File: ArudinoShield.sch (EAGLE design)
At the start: 25 parts, among them IC1 L298

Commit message: added ground plane, updated layout
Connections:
- removed net N$13: B1.GND@0, HC05.3, R2.1
- net GND: now also B1.GND@0, HC05.3, R2.1
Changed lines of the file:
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@@
-</segment>
-</net>
-<net name="N$13" class="0">
-<segment>
-<wire x1="109.22" y1="73.66" x2="109.22" y2="17.78" width="0.1524" layer="91"/>
-<wire x1="109.22" y1="17.78" x2="83.82" y2="17.78" width="0.1524" layer="91"/>
-<pinref part="B1" gate="G$1" pin="GND@0"/>
-<wire x1="83.82" y1="17.78" x2="50.8" y2="17.78" width="0.1524" layer="91"/>
-<wire x1="50.8" y1="17.78" x2="50.8" y2="30.48" width="0.1524" layer="91"/>
-<pinref part="R2" gate="G$1" pin="1"/>
-<wire x1="83.82" y1="27.94" x2="83.82" y2="17.78" width="0.1524" layer="91"/>
-<junction x="83.82" y="17.78"/>
-<pinref part="HC05" gate="A" pin="3"/>
-<wire x1="114.3" y1="73.66" x2="109.22" y2="73.66" width="0.1524" layer="91"/>
 </segment>
 </net>
@@
 <junction x="45.72" y="30.48"/>
 </segment>
-</net>
+<segment>
+<wire x1="109.22" y1="73.66" x2="109.22" y2="17.78" width="0.1524" layer="91"/>
+<wire x1="109.22" y1="17.78" x2="83.82" y2="17.78" width="0.1524" layer="91"/>
+<pinref part="B1" gate="G$1" pin="GND@0"/>
+<wire x1="83.82" y1="17.78" x2="50.8" y2="17.78" width="0.1524" layer="91"/>
+<wire x1="50.8" y1="17.78" x2="50.8" y2="30.48" width="0.1524" layer="91"/>
+<pinref part="R2" gate="G$1" pin="1"/>
+<wire x1="83.82" y1="27.94" x2="83.82" y2="17.78" width="0.1524" layer="91"/>
+<junction x="83.82" y="17.78"/>
+<pinref part="HC05" gate="A" pin="3"/>
+<wire x1="114.3" y1="73.66" x2="109.22" y2="73.66" width="0.1524" layer="91"/>
+</segment>
+</net>

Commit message: updated board and previews
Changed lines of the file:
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@@
 <pinref part="HC05" gate="A" pin="3"/>
 <wire x1="114.3" y1="73.66" x2="109.22" y2="73.66" width="0.1524" layer="91"/>
+<label x="50.8" y="17.78" size="1.6764" layer="95"/>
 </segment>
 </net>

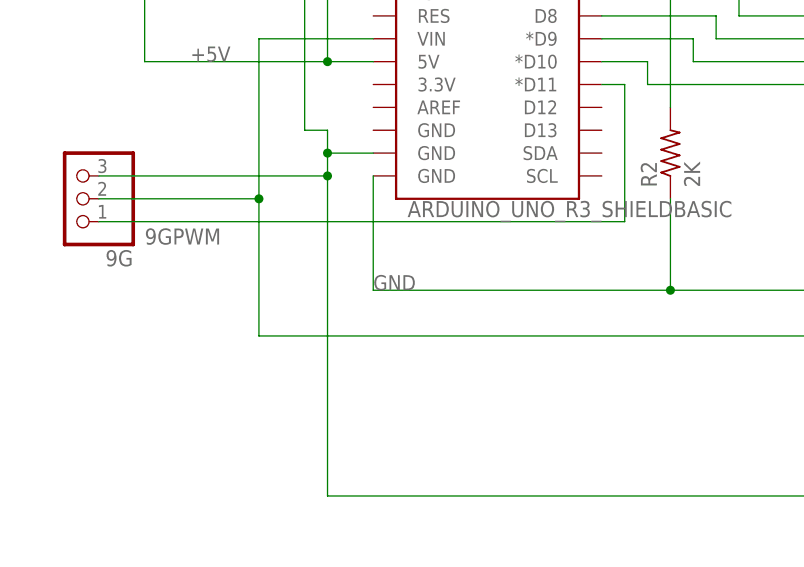
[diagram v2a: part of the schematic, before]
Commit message: fixed L298 pin 8 not being reliably grounded
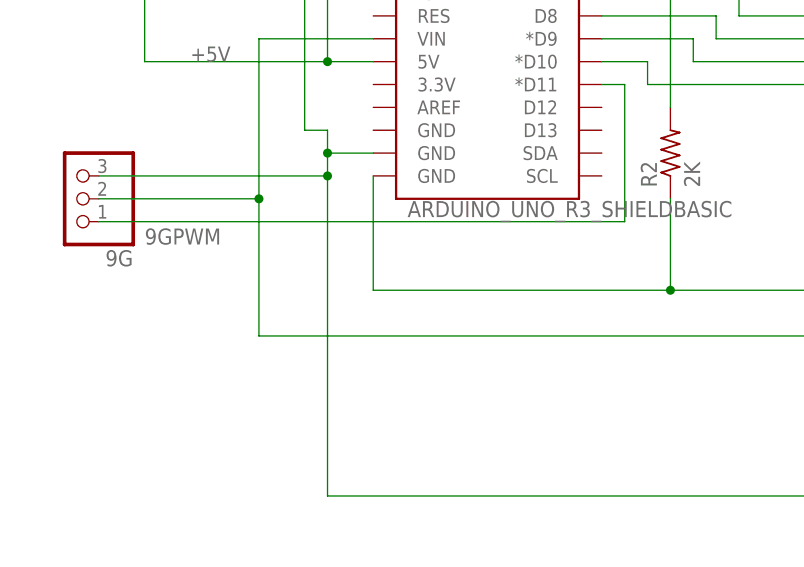
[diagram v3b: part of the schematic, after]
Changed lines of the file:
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@@
 <pinref part="HC05" gate="A" pin="3"/>
 <wire x1="114.3" y1="73.66" x2="109.22" y2="73.66" width="0.1524" layer="91"/>
-<label x="50.8" y="17.78" size="1.6764" layer="95"/>
 </segment>
 </net>

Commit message: By hand rework of board layout, no vias
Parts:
- R1: device adafruit:R-US_0207/7 -> rcl:R-US_0207/10
- R2: value 2K -> 2k; device adafruit:R-US_0207/7 -> rcl:R-US_0207/10
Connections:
- new net +5VIN: B1.VIN, C2.1, IC1.VCC, R3.2, VREG.VOUT
- net +5V: no longer B1.VIN, C2.1, IC1.VCC, R3.2, VREG.VOUT
- net 9GPWM: now also B1.*D3; no longer B1.*D11
- net ENA: now also B1.*D11; no longer B1.*D5
- net ENB: now also B1.*D9; no longer B1.*D10
- net GND: now also VIN.2; no longer VIN.1
- net IN1: now also B1.D12; no longer B1.*D6
- net IN2: now also B1.*D10; no longer B1.D7
- net IN4: now also B1.D7; no longer B1.*D9
- net N$11: now also R1.2; no longer R1.1
- net N$14: now also R1.1; no longer R1.2
- net VIN: now also VIN.1; no longer VIN.2
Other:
- moved on the sheet: R1

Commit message: minor changes, updated images
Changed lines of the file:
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@@
 <segment>
 <pinref part="IC1" gate="L298" pin="INPUT1"/>
-<label x="124.46" y="50.8" size="1.6764" layer="95"/>
-<wire x1="129.54" y1="50.8" x2="88.9" y2="50.8" width="0.1524" layer="91"/>
-<wire x1="88.9" y1="50.8" x2="88.9" y2="38.1" width="0.1524" layer="91"/>
+<label x="73.66" y="38.1" size="1.6764" layer="95"/>
+<wire x1="129.54" y1="50.8" x2="111.76" y2="50.8" width="0.1524" layer="91"/>
+<wire x1="111.76" y1="50.8" x2="111.76" y2="38.1" width="0.1524" layer="91"/>
 <pinref part="B1" gate="G$1" pin="D12"/>
-<wire x1="88.9" y1="38.1" x2="76.2" y2="38.1" width="0.1524" layer="91"/>
+<wire x1="111.76" y1="38.1" x2="76.2" y2="38.1" width="0.1524" layer="91"/>
 </segment>
 </net>
@@
 <pinref part="IC1" gate="L298" pin="ENABLE_A"/>
 <wire x1="121.92" y1="58.42" x2="129.54" y2="58.42" width="0.1524" layer="91"/>
-<label x="124.46" y="58.42" size="1.6764" layer="95"/>
+<label x="73.66" y="40.64" size="1.6764" layer="95"/>
 </segment>
 </net>
@@
 <segment>
 <pinref part="IC1" gate="L298" pin="ENABLE_B"/>
-<label x="124.46" y="55.88" size="1.6764" layer="95"/>
+<label x="73.66" y="45.72" size="1.6764" layer="95"/>
 <wire x1="129.54" y1="55.88" x2="116.84" y2="55.88" width="0.1524" layer="91"/>
 <wire x1="116.84" y1="55.88" x2="116.84" y2="45.72" width="0.1524" layer="91"/>
@@
 <segment>
 <pinref part="IC1" gate="L298" pin="INPUT2"/>
-<label x="124.46" y="48.26" size="1.6764" layer="95"/>
-<wire x1="129.54" y1="48.26" x2="119.38" y2="48.26" width="0.1524" layer="91"/>
-<wire x1="119.38" y1="48.26" x2="119.38" y2="43.18" width="0.1524" layer="91"/>
+<label x="73.66" y="43.18" size="1.6764" layer="95"/>
+<wire x1="129.54" y1="48.26" x2="93.98" y2="48.26" width="0.1524" layer="91"/>
+<wire x1="93.98" y1="48.26" x2="93.98" y2="43.18" width="0.1524" layer="91"/>
 <pinref part="B1" gate="G$1" pin="*D10"/>
-<wire x1="119.38" y1="43.18" x2="76.2" y2="43.18" width="0.1524" layer="91"/>
+<wire x1="93.98" y1="43.18" x2="76.2" y2="43.18" width="0.1524" layer="91"/>
 </segment>
 </net>
@@
 <segment>
 <pinref part="IC1" gate="L298" pin="INPUT3"/>
-<label x="124.46" y="45.72" size="1.6764" layer="95"/>
-<wire x1="129.54" y1="45.72" x2="93.98" y2="45.72" width="0.1524" layer="91"/>
-<wire x1="93.98" y1="45.72" x2="93.98" y2="48.26" width="0.1524" layer="91"/>
+<label x="73.66" y="48.26" size="1.6764" layer="95"/>
+<wire x1="129.54" y1="45.72" x2="119.38" y2="45.72" width="0.1524" layer="91"/>
+<wire x1="119.38" y1="45.72" x2="119.38" y2="48.26" width="0.1524" layer="91"/>
 <pinref part="B1" gate="G$1" pin="D8"/>
-<wire x1="93.98" y1="48.26" x2="76.2" y2="48.26" width="0.1524" layer="91"/>
+<wire x1="119.38" y1="48.26" x2="76.2" y2="48.26" width="0.1524" layer="91"/>
 </segment>
 </net>
@@
 <segment>
 <pinref part="IC1" gate="L298" pin="INPUT4"/>
-<label x="124.46" y="43.18" size="1.6764" layer="95"/>
-<wire x1="129.54" y1="43.18" x2="86.36" y2="43.18" width="0.1524" layer="91"/>
-<wire x1="86.36" y1="43.18" x2="86.36" y2="50.8" width="0.1524" layer="91"/>
+<label x="73.66" y="50.8" size="1.6764" layer="95"/>
+<wire x1="129.54" y1="43.18" x2="99.06" y2="43.18" width="0.1524" layer="91"/>
+<wire x1="99.06" y1="43.18" x2="99.06" y2="50.8" width="0.1524" layer="91"/>
 <pinref part="B1" gate="G$1" pin="D7"/>
-<wire x1="86.36" y1="50.8" x2="76.2" y2="50.8" width="0.1524" layer="91"/>
+<wire x1="99.06" y1="50.8" x2="76.2" y2="50.8" width="0.1524" layer="91"/>
 </segment>
 </net>

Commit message: minor board changes
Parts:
- renumbered VREG to U1
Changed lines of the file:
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@@
 <part name="R3" library="rcl" library_urn="urn:adsk.eagle:library:334" deviceset="R-US_" device="0207/10" package3d_urn="urn:adsk.eagle:package:23491/2" value="1k"/>
 <part name="LED1" library="led" library_urn="urn:adsk.eagle:library:259" deviceset="LED" device="5MM" package3d_urn="urn:adsk.eagle:package:15799/2"/>
-<part name="VREG" library="burr-brown" library_urn="urn:adsk.eagle:library:111" deviceset="REG1117" device="" package3d_urn="urn:adsk.eagle:package:4940/1"/>
+<part name="U1" library="burr-brown" library_urn="urn:adsk.eagle:library:111" deviceset="REG1117" device="" package3d_urn="urn:adsk.eagle:package:4940/1"/>
 <part name="VIN" library="con-amp" library_urn="urn:adsk.eagle:library:127" deviceset="MTA02-156" device="" package3d_urn="urn:adsk.eagle:package:8081562/1"/>
 <part name="OUT3" library="con-amp" library_urn="urn:adsk.eagle:library:127" deviceset="MTA02-156" device="" package3d_urn="urn:adsk.eagle:package:8081562/1"/>
@@
 <attribute name="VALUE" x="173.355" y="-4.572" size="1.778" layer="96" rot="R90"/>
 </instance>
-<instance part="VREG" gate="G$1" x="139.7" y="12.7" smashed="yes">
+<instance part="U1" gate="G$1" x="139.7" y="12.7" smashed="yes">
 <attribute name="NAME" x="132.08" y="18.415" size="1.778" layer="95" ratio="10"/>
 <attribute name="VALUE" x="134.62" y="15.24" size="1.778" layer="96" ratio="10"/>
@@
 <wire x1="175.26" y1="30.48" x2="175.26" y2="-12.7" width="0.1524" layer="91"/>
 <junction x="175.26" y="-12.7"/>
-<pinref part="VREG" gate="G$1" pin="GND"/>
+<pinref part="U1" gate="G$1" pin="GND"/>
 <pinref part="B1" gate="G$1" pin="GND@1"/>
 <wire x1="50.8" y1="33.02" x2="45.72" y2="33.02" width="0.1524" layer="91"/>
@@
 <wire x1="246.38" y1="93.98" x2="215.9" y2="93.98" width="0.8128" layer="91"/>
 <junction x="215.9" y="93.98"/>
-<pinref part="VREG" gate="G$1" pin="VIN"/>
+<pinref part="U1" gate="G$1" pin="VIN"/>
 <wire x1="127" y1="12.7" x2="121.92" y2="12.7" width="0.8128" layer="91"/>
 <pinref part="IC1" gate="L298" pin="VS"/>
@@
 <wire x1="157.48" y1="10.16" x2="157.48" y2="12.7" width="0.1524" layer="91"/>
 <junction x="157.48" y="12.7"/>
-<pinref part="VREG" gate="G$1" pin="VOUT"/>
+<pinref part="U1" gate="G$1" pin="VOUT"/>
 <pinref part="B1" gate="G$1" pin="VIN"/>
 <wire x1="50.8" y1="45.72" x2="38.1" y2="45.72" width="0.1524" layer="91"/>

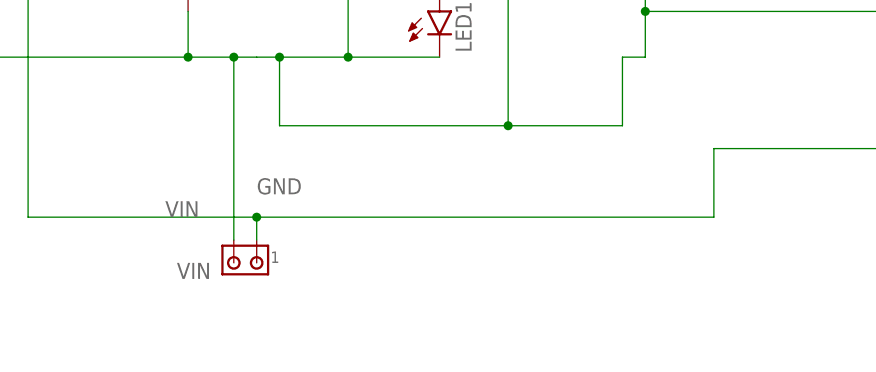
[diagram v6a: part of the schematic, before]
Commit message: updated schematic and board to use DC jack
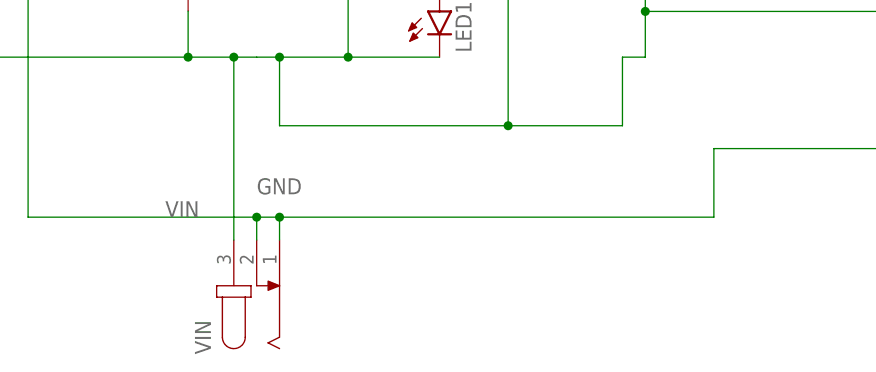
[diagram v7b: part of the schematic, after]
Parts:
- VIN: device con-amp:MTA02-156 -> con-jack:JACK-PLUG1
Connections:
- net GND: now also VIN.3; no longer VIN.2
- net VIN: now also VIN.2
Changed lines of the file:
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@@
 <part name="LED1" library="led" library_urn="urn:adsk.eagle:library:259" deviceset="LED" device="5MM" package3d_urn="urn:adsk.eagle:package:15799/2"/>
 <part name="U1" library="burr-brown" library_urn="urn:adsk.eagle:library:111" deviceset="REG1117" device="" package3d_urn="urn:adsk.eagle:package:4940/1"/>
-<part name="VIN" library="con-amp" library_urn="urn:adsk.eagle:library:127" deviceset="MTA02-156" device="" package3d_urn="urn:adsk.eagle:package:8081562/1"/>
 <part name="OUT3" library="con-amp" library_urn="urn:adsk.eagle:library:127" deviceset="MTA02-156" device="" package3d_urn="urn:adsk.eagle:package:8081562/1"/>
 <part name="OUT4" library="con-amp" library_urn="urn:adsk.eagle:library:127" deviceset="MTA02-156" device="" package3d_urn="urn:adsk.eagle:package:8081562/1"/>
@@
 <part name="R2" library="rcl" library_urn="urn:adsk.eagle:library:334" deviceset="R-US_" device="0207/10" package3d_urn="urn:adsk.eagle:package:23491/2" value="2k"/>
 <part name="R1" library="rcl" library_urn="urn:adsk.eagle:library:334" deviceset="R-US_" device="0207/10" package3d_urn="urn:adsk.eagle:package:23491/2" value="1k"/>
+<part name="VIN" library="con-jack" library_urn="urn:adsk.eagle:library:154" deviceset="JACK-PLUG" device="1" package3d_urn="urn:adsk.eagle:package:7494/1"/>
 </parts>
 <sheets>
@@
 <attribute name="VALUE" x="134.62" y="15.24" size="1.778" layer="96" ratio="10"/>
 </instance>
-<instance part="VIN" gate="G$1" x="147.32" y="-27.94" smashed="yes" rot="R180">
-<attribute name="NAME" x="142.24" y="-27.94" size="1.778" layer="95" rot="R180"/>
-<attribute name="VALUE" x="142.24" y="-24.13" size="1.778" layer="96" rot="R180"/>
-</instance>
 <instance part="OUT3" gate="G$1" x="233.68" y="45.72" smashed="yes" rot="R270">
 <attribute name="NAME" x="236.22" y="45.72" size="1.778" layer="95" rot="R270"/>
@@
 <attribute name="NAME" x="95.25" y="67.0814" size="1.778" layer="95" rot="R180"/>
 <attribute name="VALUE" x="95.25" y="71.882" size="1.778" layer="96" rot="R180"/>
+</instance>
+<instance part="VIN" gate="G$1" x="147.32" y="-30.48" smashed="yes" rot="R90">
+<attribute name="NAME" x="142.24" y="-38.1" size="1.778" layer="95" rot="R90"/>
+<attribute name="VALUE" x="152.4" y="-38.1" size="1.778" layer="96" rot="R90"/>
 </instance>
 </instances>
@@
 <junction x="50.8" y="17.78"/>
 <junction x="45.72" y="17.78"/>
-<pinref part="VIN" gate="G$1" pin="2"/>
 <wire x1="144.78" y1="-25.4" x2="144.78" y2="-5.08" width="0.1524" layer="91"/>
 <junction x="144.78" y="-5.08"/>
+<pinref part="VIN" gate="G$1" pin="3"/>
 </segment>
 </net>
@@
 <segment>
 <wire x1="198.12" y1="-15.24" x2="198.12" y2="-22.86" width="0.8128" layer="91"/>
-<wire x1="198.12" y1="-22.86" x2="147.32" y2="-22.86" width="0.8128" layer="91"/>
+<wire x1="198.12" y1="-22.86" x2="149.86" y2="-22.86" width="0.8128" layer="91"/>
+<wire x1="149.86" y1="-22.86" x2="147.32" y2="-22.86" width="0.8128" layer="91"/>
 <wire x1="147.32" y1="-22.86" x2="121.92" y2="-22.86" width="0.8128" layer="91"/>
 <wire x1="121.92" y1="-22.86" x2="121.92" y2="12.7" width="0.8128" layer="91"/>
@@
 <wire x1="160.02" y1="63.5" x2="160.02" y2="93.98" width="0.8128" layer="91"/>
 <label x="137.16" y="-22.86" size="1.778" layer="95"/>
-<pinref part="VIN" gate="G$1" pin="1"/>
 <wire x1="147.32" y1="-25.4" x2="147.32" y2="-22.86" width="0.1524" layer="91"/>
 <junction x="147.32" y="-22.86"/>
-</segment>
-</net>
+<pinref part="VIN" gate="G$1" pin="2"/>
+<pinref part="VIN" gate="G$1" pin="1"/>
+<wire x1="149.86" y1="-25.4" x2="149.86" y2="-22.86" width="0.1524" layer="91"/>
+<junction x="149.86" y="-22.86"/>
+</segment>
+</net>
